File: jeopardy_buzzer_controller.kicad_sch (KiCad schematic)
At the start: 10 parts, among them J1 XLR4_Ground, J2 XLR4_Ground, J3 XLR4_Ground, J4 XLR4_Ground, J5 XLR4_Ground, J6 XLR4_Ground, J7 XLR4_Ground, J8 XLR4_Ground, SW1 RESET, U1 ProMicro

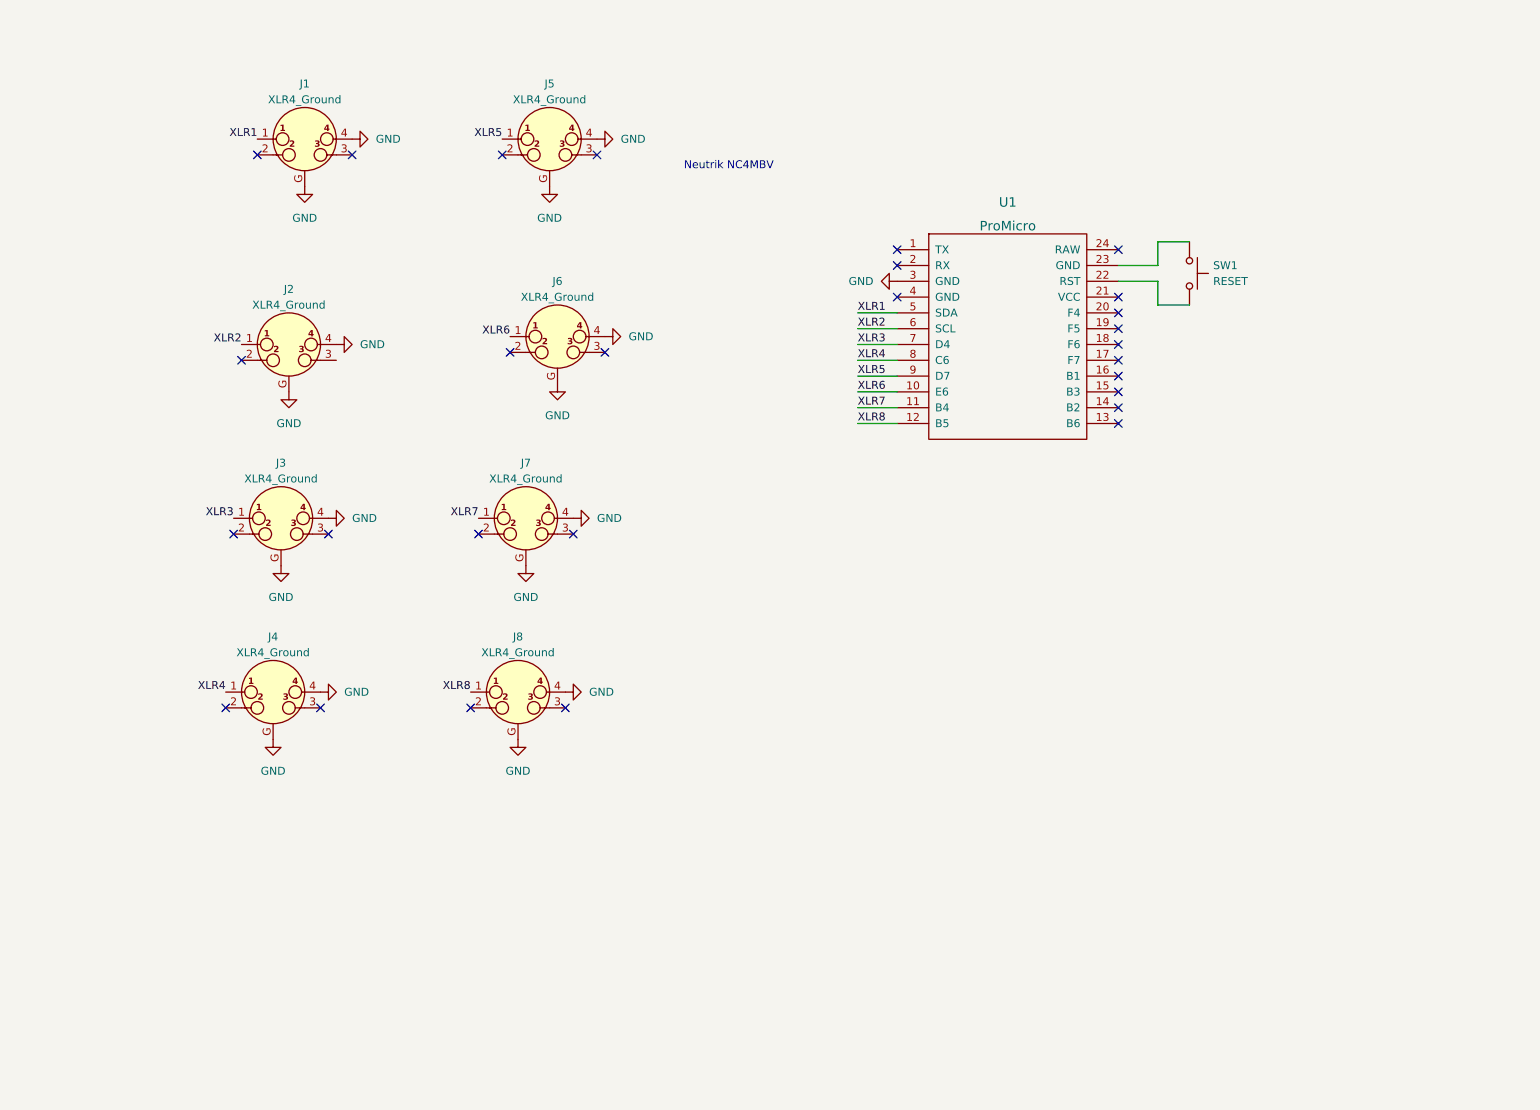
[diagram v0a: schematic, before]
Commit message: Add power LED, enable switch, enable LED
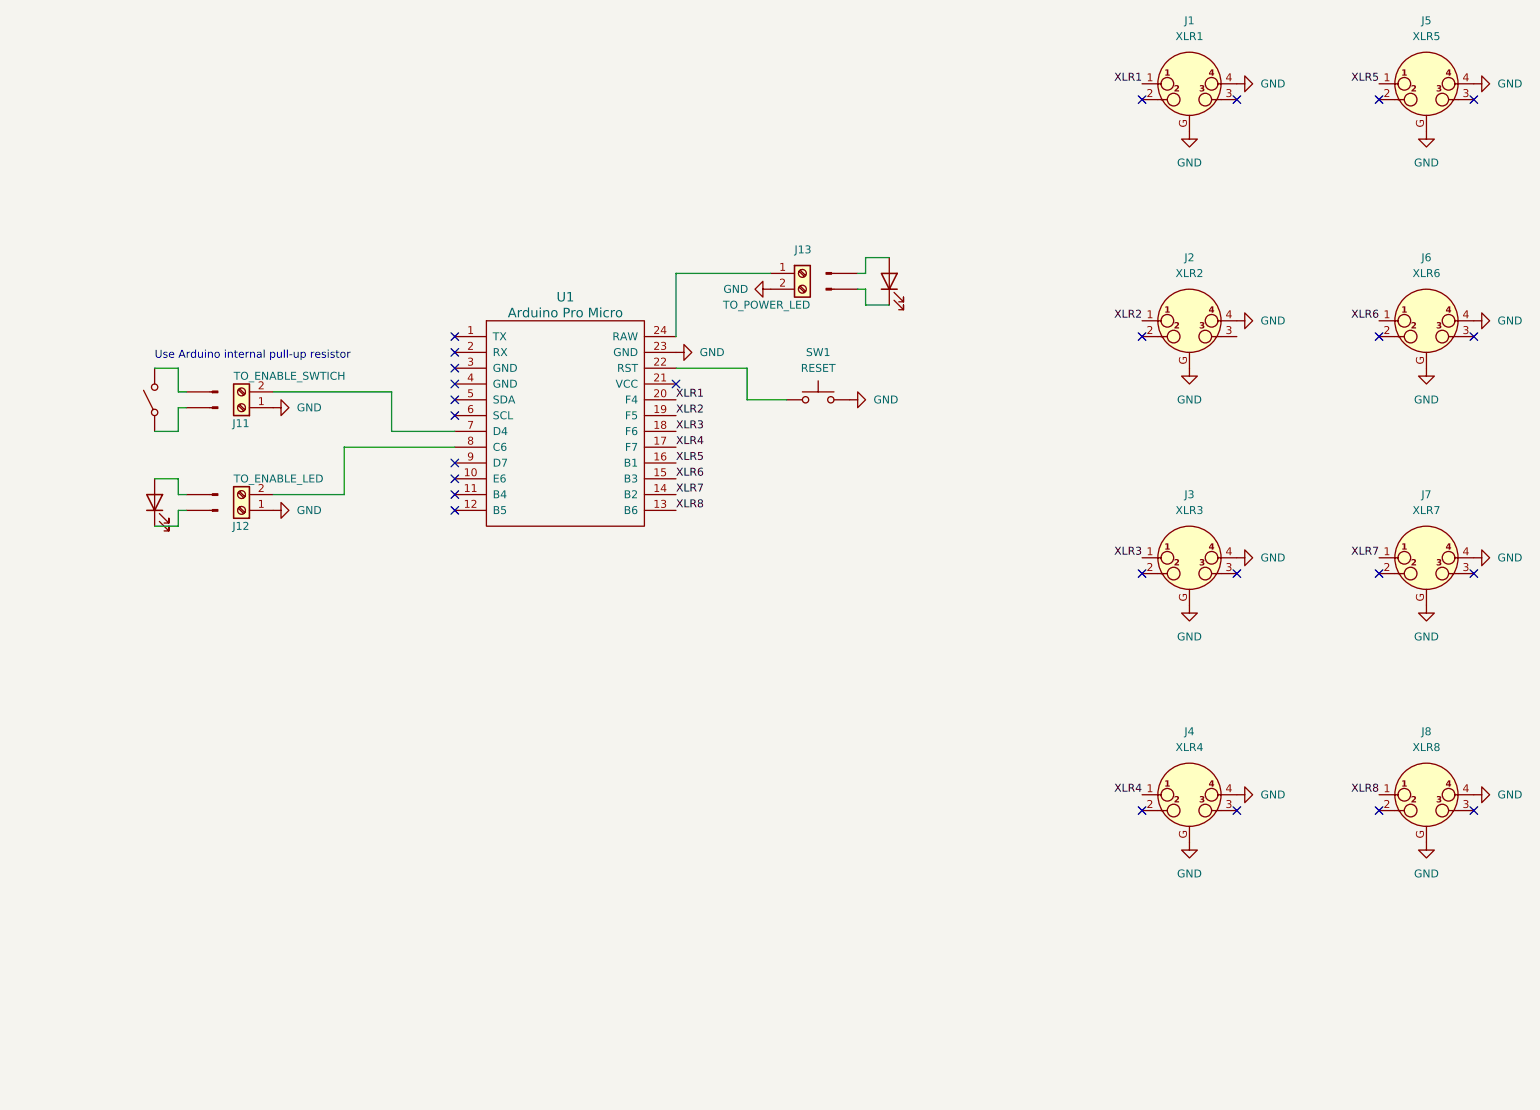
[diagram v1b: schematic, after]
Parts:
- added D1: Power_LED, symbol Device:LED
- added D2: Enable_LED, symbol Device:LED
- added J10, J14, J9: Conn_01x02_Male, symbol Connector:Conn_01x02_Male
- added J11: TO_ENABLE_SWTICH, TerminalBlock_Phoenix:TerminalBlock_Phoenix_MKDS-1,5-2-5.08_1x02_P5.08mm_Horizontal, symbol Connector:Screw_Terminal_01x02
- added J12: TO_ENABLE_LED, TerminalBlock_Phoenix:TerminalBlock_Phoenix_MKDS-1,5-2-5.08_1x02_P5.08mm_Horizontal, symbol Connector:Screw_Terminal_01x02
- added J13: TO_POWER_LED, TerminalBlock_Phoenix:TerminalBlock_Phoenix_MKDS-1,5-2-5.08_1x02_P5.08mm_Horizontal, symbol Connector:Screw_Terminal_01x02
- added SW2: Enable_switch, symbol Switch:SW_SPST
- J1: value XLR4_Ground -> XLR1
- J2: value XLR4_Ground -> XLR2
- J3: value XLR4_Ground -> XLR3
- J4: value XLR4_Ground -> XLR4
- J5: value XLR4_Ground -> XLR5
- J6: value XLR4_Ground -> XLR6
- J7: value XLR4_Ground -> XLR7
- J8: value XLR4_Ground -> XLR8
- U1: value ProMicro -> Arduino Pro Micro
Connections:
- net GND: now also SW1.2, U1.23 (GND), J11.1 (Pin_1), J12.1 (Pin_1), J13.2 (Pin_2); no longer U1.3 (GND)
- net XLR1: now also U1.20 (F4); no longer U1.5 (SDA)
- net XLR2: now also U1.19 (F5); no longer U1.6 (SCL)
- net XLR3: now also U1.18 (F6); no longer U1.7 (D4)
- net XLR4: now also U1.17 (F7); no longer U1.8 (C6)
- net XLR5: now also U1.16 (B1); no longer U1.9 (D7)
- net XLR6: now also U1.15 (B3); no longer U1.10 (E6)
- net XLR7: now also U1.14 (B2); no longer U1.11 (B4)
- net XLR8: now also U1.13 (B6); no longer U1.12 (B5)
- net at U1.22 (RST): now also SW1.1; no longer SW1.2
- net at U1.24 (RAW): now also J13.1 (Pin_1)
- new net: J11.2 (Pin_2), U1.7 (D4)
- new net: J12.2 (Pin_2), U1.8 (C6)
- new net: D1.2 (A), J14.1 (Pin_1)
- new net: D1.1 (K), J14.2 (Pin_2)
- new net: D2.1 (K), J10.1 (Pin_1)
- new net: D2.2 (A), J10.2 (Pin_2)
- new net: J9.1 (Pin_1), SW2.1 (A)
- new net: J9.2 (Pin_2), SW2.2 (B)
- no-connect marks 28 -> 26
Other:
- note added: "Use Arduino internal pull-up resistor"
- note removed: "Neutrik NC4MBV"
- moved on the sheet: J1, J2, J3, J4, J5, J6, J7, J8, SW1, U1

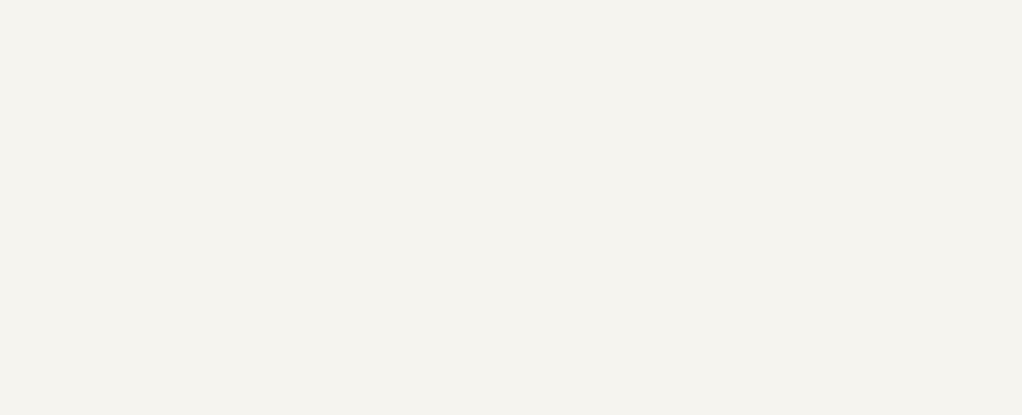
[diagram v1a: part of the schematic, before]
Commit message: Add CERN OHL2-S license
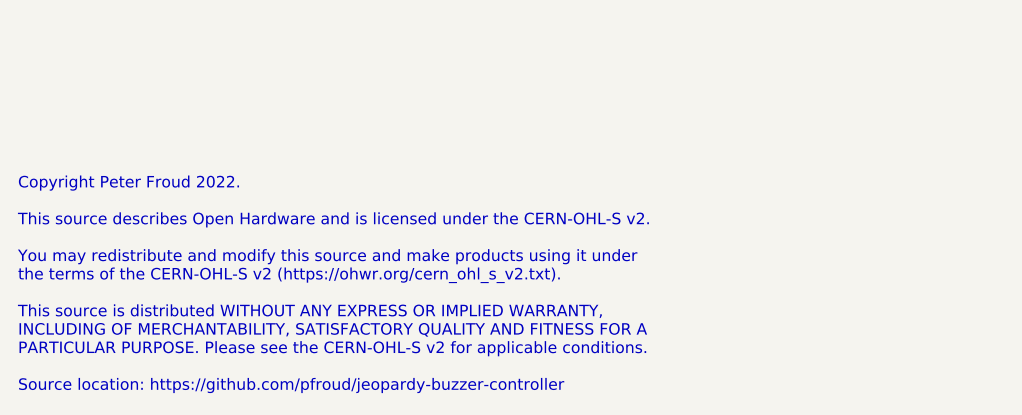
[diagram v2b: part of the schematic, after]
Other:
- note added: "Copyright Peter Froud 2022. This source describes Open Hardware and is licensed under the CERN-OHL-S v2. You may redistribute and modify this source and make products using it under the terms of the CERN-OHL-S v2 (https://ohwr.org/cern_ohl_s_v2.txt). This source is distributed WITHOUT ANY EXPRESS OR IMPLIED WARRANTY, INCLUDING OF MERCHANTABILITY, SATISFACTORY QUALITY AND FITNESS FOR A PARTICULAR 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"
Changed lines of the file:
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@@
+    (effects (font (size 1.27 1.27)) (justify left bottom))
+  )
+  (text "Copyright Peter Froud 2022.\n\nThis source describes Open Hardware and is licensed under the CERN-OHL-S v2.\n\nYou may redistribute and modify this source and make products using it under\nthe terms of the CERN-OHL-S v2 (https://ohwr.org/cern_ohl_s_v2.txt).\n\nThis source is distributed WITHOUT ANY EXPRESS OR IMPLIED WARRANTY,\nINCLUDING OF MERCHANTABILITY, SATISFACTORY QUALITY AND FITNESS FOR A\nPARTICULAR PURPOSE. Please see the CERN-OHL-S v2 for applicable conditions. \n\nSource location: https://github.com/pfroud/jeopardy-buzzer-controller"
+    (at 13.97 195.58 0)
     (effects (font (size 1.27 1.27)) (justify left bottom))
   )
